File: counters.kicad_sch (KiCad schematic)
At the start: 20 parts, among them U10 74LV04, U11 74HC109, U12 74LV163, U13 74LV163, U14 74AHC30, U16 74VHC30, U18 74AHC30, U19 74VHC30, U20 74LV163, U21 74LV163, U22 74LV163, U23 74VHC30, U24 74HC109, U25 74VHC30, U26 74VHC30, U27 74VHC30, U28 74LV04, U29 74LV08, U8 74LV163, X1 25.175MHz

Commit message: cleanup
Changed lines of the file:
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@@
     (effects (font (size 1.27 1.27)) (justify left))
   )
-  (hierarchical_label "Row" (shape output) (at 261.62 69.85 0) (fields_autoplaced)
+  (hierarchical_label "Row[0..9]" (shape output) (at 261.62 69.85 0) (fields_autoplaced)
     (effects (font (size 1.27 1.27)) (justify left))
   )
@@
     (effects (font (size 1.27 1.27)) (justify left))
   )
-  (hierarchical_label "Col" (shape output) (at 133.35 71.12 0) (fields_autoplaced)
+  (hierarchical_label "Col[0..9]" (shape output) (at 133.35 71.12 0) (fields_autoplaced)
     (effects (font (size 1.27 1.27)) (justify left))
   )

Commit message: remove 3390, cleanup
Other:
- moved on the sheet: U12, U13, U20, U21, U22, U8

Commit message: misc fixes, start on pcb
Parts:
- removed unit 7 of U10
- removed unit 3 of U11
- removed unit 2 of U14
- removed unit 2 of U16
- removed unit 2 of U18
- removed unit 2 of U19
- removed unit 2 of U23
- removed unit 3 of U24
- removed unit 2 of U25
- removed unit 2 of U26
- removed unit 2 of U27
- removed unit 7 of U28
- removed unit 5 of U29
- added C1 (x7): 0.1u, Capacitor_SMD:C_1206_3216Metric_Pad1.33x1.80mm_HandSolder, symbol Device:C
- U10: renamed from U14; footprint (none) -> Package_SO:SOIC-14_3.9x8.7mm_P1.27mm
- U11: renamed from U18; footprint (none) -> Package_SO:SOIC-14_3.9x8.7mm_P1.27mm
- U12: renamed from U16; value 74VHC30 -> 74AHC30; footprint (none) -> Package_SO:SOIC-14_3.9x8.7mm_P1.27mm
- U13: renamed from U19; value 74VHC30 -> 74AHC30; footprint (none) -> Package_SO:SOIC-14_3.9x8.7mm_P1.27mm
- U14: renamed from U8; footprint (none) -> Package_SO:SOIC-16_3.9x9.9mm_P1.27mm
- U15: renamed from U10; footprint (none) -> Package_SO:SOIC-14_3.9x8.7mm_P1.27mm
- U16: renamed from U11; value 74HC109 -> 74AC109; footprint (none) -> Package_SO:SOIC-16_3.9x9.9mm_P1.27mm
- U17: renamed from U12; footprint (none) -> Package_SO:SOIC-16_3.9x9.9mm_P1.27mm
- U18: renamed from U28; footprint (none) -> Package_SO:SOIC-14_3.9x8.7mm_P1.27mm
- U19: renamed from U29; footprint (none) -> Package_SO:SOIC-14_3.9x8.7mm_P1.27mm
- U20: renamed from U13; footprint (none) -> Package_SO:SOIC-16_3.9x9.9mm_P1.27mm
- U21: renamed from U23; value 74VHC30 -> 74AHC30; footprint (none) -> Package_SO:SOIC-14_3.9x8.7mm_P1.27mm
- U22: renamed from U25; value 74VHC30 -> 74AHC30; footprint (none) -> Package_SO:SOIC-14_3.9x8.7mm_P1.27mm
- U23: renamed from U26; value 74VHC30 -> 74AHC30; footprint (none) -> Package_SO:SOIC-14_3.9x8.7mm_P1.27mm
- U24: renamed from U27; value 74VHC30 -> 74AHC30; footprint (none) -> Package_SO:SOIC-14_3.9x8.7mm_P1.27mm
- U25: renamed from U24; value 74HC109 -> 74AC109; footprint (none) -> Package_SO:SOIC-16_3.9x9.9mm_P1.27mm
- U26: renamed from U20; footprint (none) -> Package_SO:SOIC-16_3.9x9.9mm_P1.27mm
- U27: renamed from U21; footprint (none) -> Package_SO:SOIC-16_3.9x9.9mm_P1.27mm
- U28: renamed from U22; footprint (none) -> Package_SO:SOIC-16_3.9x9.9mm_P1.27mm
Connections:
- net +5V: now also C1.1, C1.1, C1.1, C1.1, C1.1, C1.1, C1.1
- net GND: now also C1.2, C1.2, C1.2, C1.2, C1.2, C1.2, C1.2
- net ~{HSync}: now reaches U16.9 (~{Q})
- net ~{VSync}: now reaches U25.9 (~{Q})
- net HSync: no longer names the net of U16.10 (Q)
- net VSync: no longer names the net of U25.10 (Q)
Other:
- note added: "Misc"
- note removed: "Power/Misc"
- moved on the sheet: X1

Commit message: pcb organization
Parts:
- added J10, J9: Conn_01x10, Connector_PinHeader_2.54mm:PinHeader_1x10_P2.54mm_Vertical, symbol Connector_Generic:Conn_01x10
- added J11, J12, J13, J14: Conn_01x03, Connector_PinHeader_2.54mm:PinHeader_1x03_P2.54mm_Vertical, symbol Connector_Generic:Conn_01x03
- added J16: Conn_01x01, Connector_PinHeader_2.54mm:PinHeader_1x01_P2.54mm_Vertical, symbol Connector_Generic:Conn_01x01
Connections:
- net Col0: now also J10.1 (Pin_1)
- net Col1: now also J10.2 (Pin_2)
- net Col2: now also J10.3 (Pin_3)
- net Col3: now also J10.4 (Pin_4)
- net Col4: now also J10.5 (Pin_5)
- net Col5: now also J10.6 (Pin_6)
- net Col6: now also J10.7 (Pin_7)
- net Col7: now also J10.8 (Pin_8)
- net Col8: now also J10.9 (Pin_9)
- net Col9: now also J10.10 (Pin_10)
- net HBlank: now also J11.1 (Pin_1)
- net HBlankClear: now also J11.3 (Pin_3)
- net HSyncSet: now also J12.2 (Pin_2)
- net PxClock: now also J16.1 (Pin_1)
- net Row0: now also J9.1 (Pin_1)
- net Row1: now also J9.2 (Pin_2)
- net Row2: now also J9.3 (Pin_3)
- net Row3: now also J9.4 (Pin_4)
- net Row4: now also J9.5 (Pin_5)
- net Row5: now also J9.6 (Pin_6)
- net Row6: now also J9.7 (Pin_7)
- net Row7: now also J9.8 (Pin_8)
- net Row8: now also J9.9 (Pin_9)
- net Row9: now also J9.10 (Pin_10)
- net VBlank: now also J13.1 (Pin_1)
- net VBlankSet: now also J13.2 (Pin_2)
- net VSyncSet: now also J14.2 (Pin_2)
- net ~{HBlankSet}: now also J11.2 (Pin_2)
- net ~{HSyncClear}: now also J12.3 (Pin_3)
- net ~{HSync}: now also J12.1 (Pin_1)
- net ~{VBlankClear}: now also J13.3 (Pin_3)
- net ~{VSyncClear}: now also J14.3 (Pin_3)
- net ~{VSync}: now also J14.1 (Pin_1)
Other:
- moved on the sheet: C1, U15E, U18E, U18F, U19D, X1

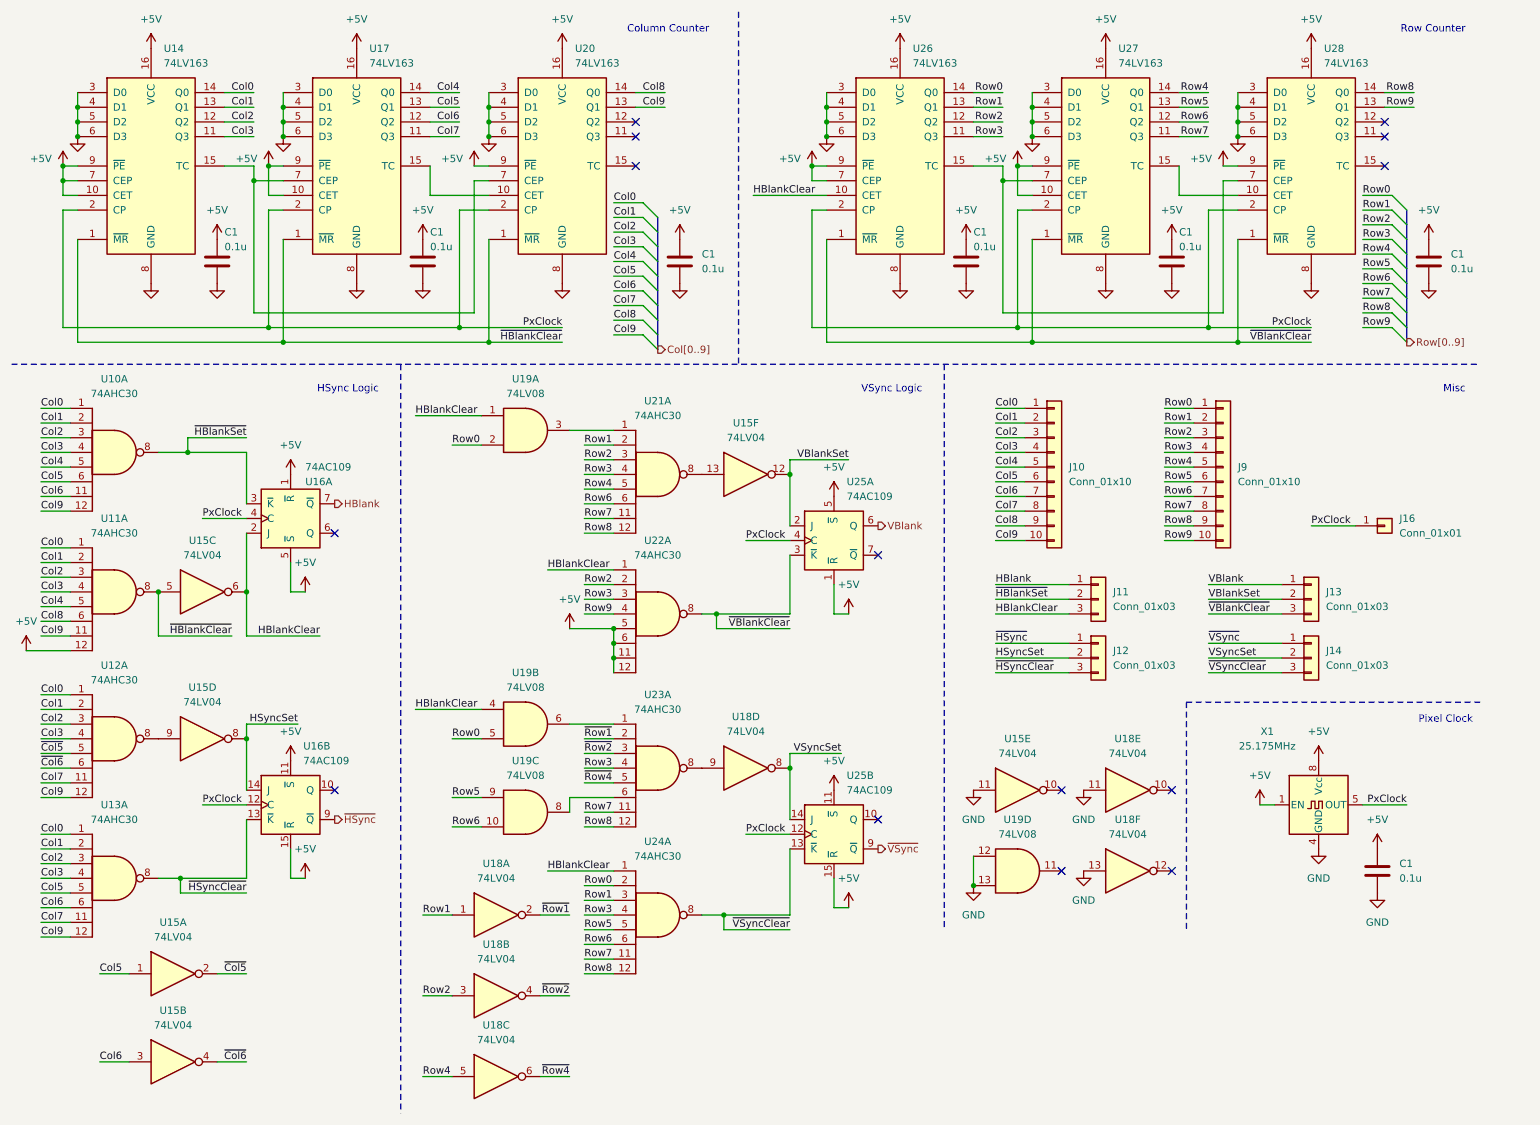
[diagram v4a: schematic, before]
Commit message: Suuuper dense routing for column counter
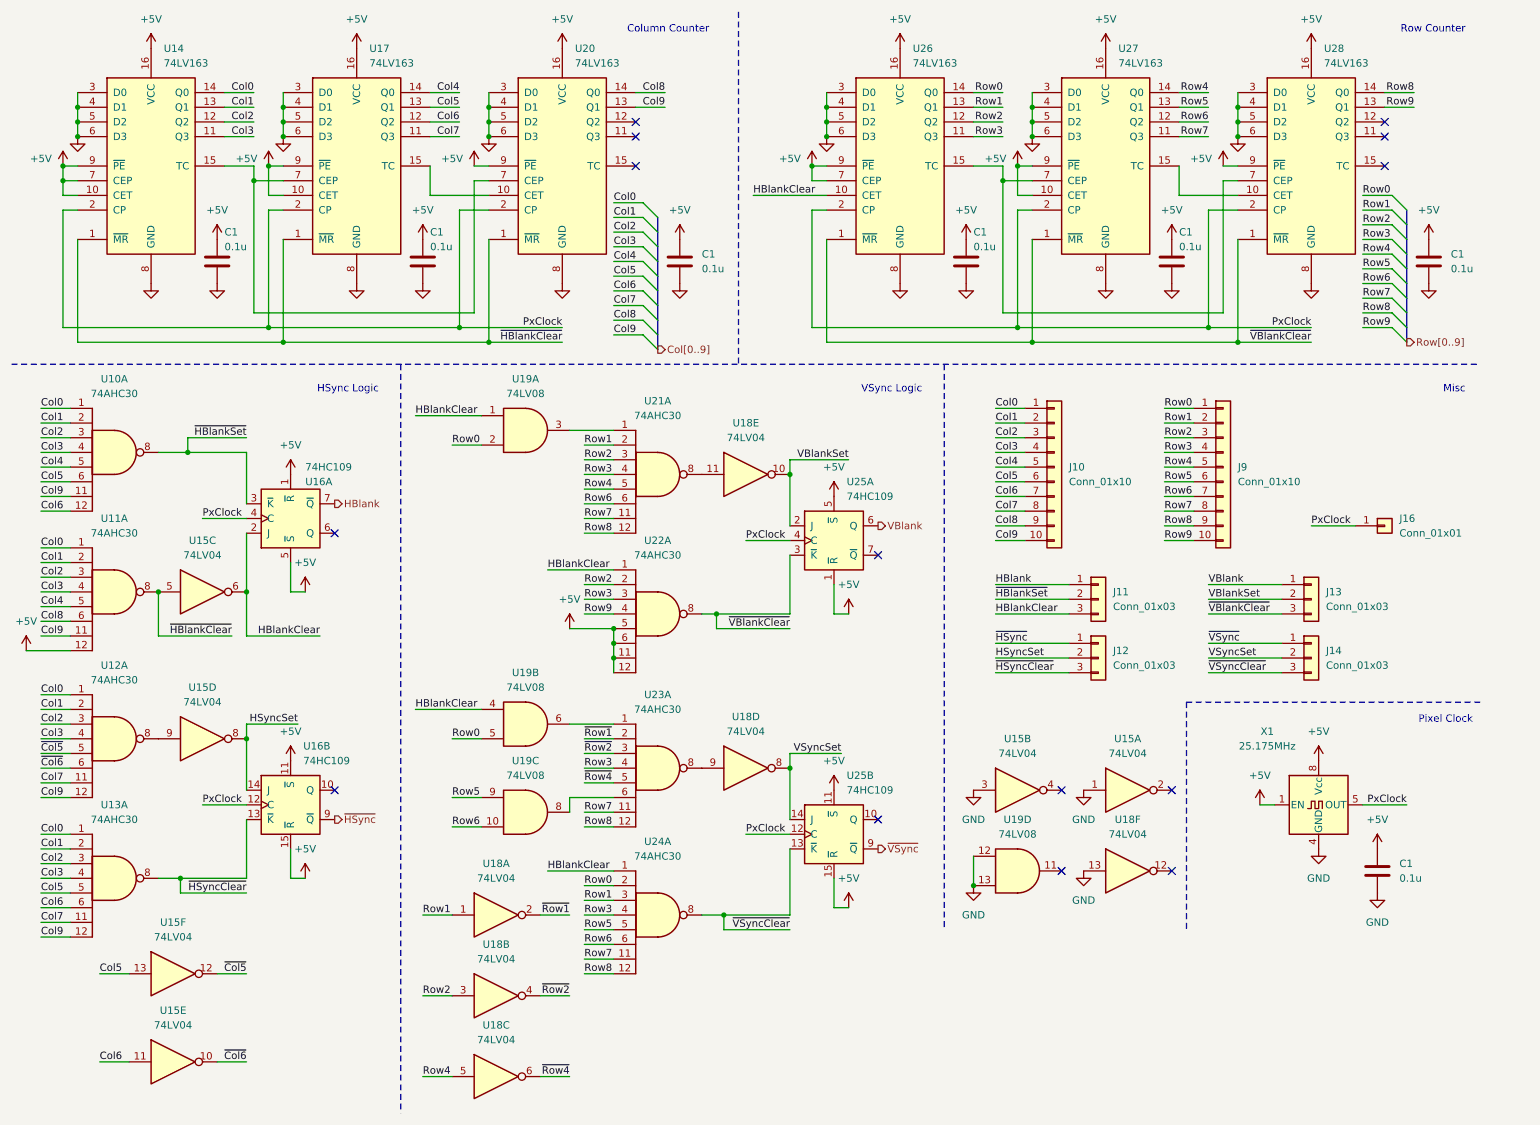
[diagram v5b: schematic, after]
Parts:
- U16, U25: value 74AC109 -> 74HC109
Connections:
- net Col5: now also U15.13; no longer U15.1
- net Col6: now also U10.12, U15.11; no longer U10.11, U15.3
- net Col9: now also U10.11; no longer U10.12
- net GND: now also U15.1, U15.3; no longer U15.11, U18.11
- net VBlankSet: now also U18.10; no longer U15.12
- net ~{Col5}: now also U15.12; no longer U15.2
- net ~{Col6}: now also U15.10; no longer U15.4
- net at U21.8: now also U18.11; no longer U15.13
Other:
- moved on the sheet: U15A, U15B, U15E, U15F, U18E

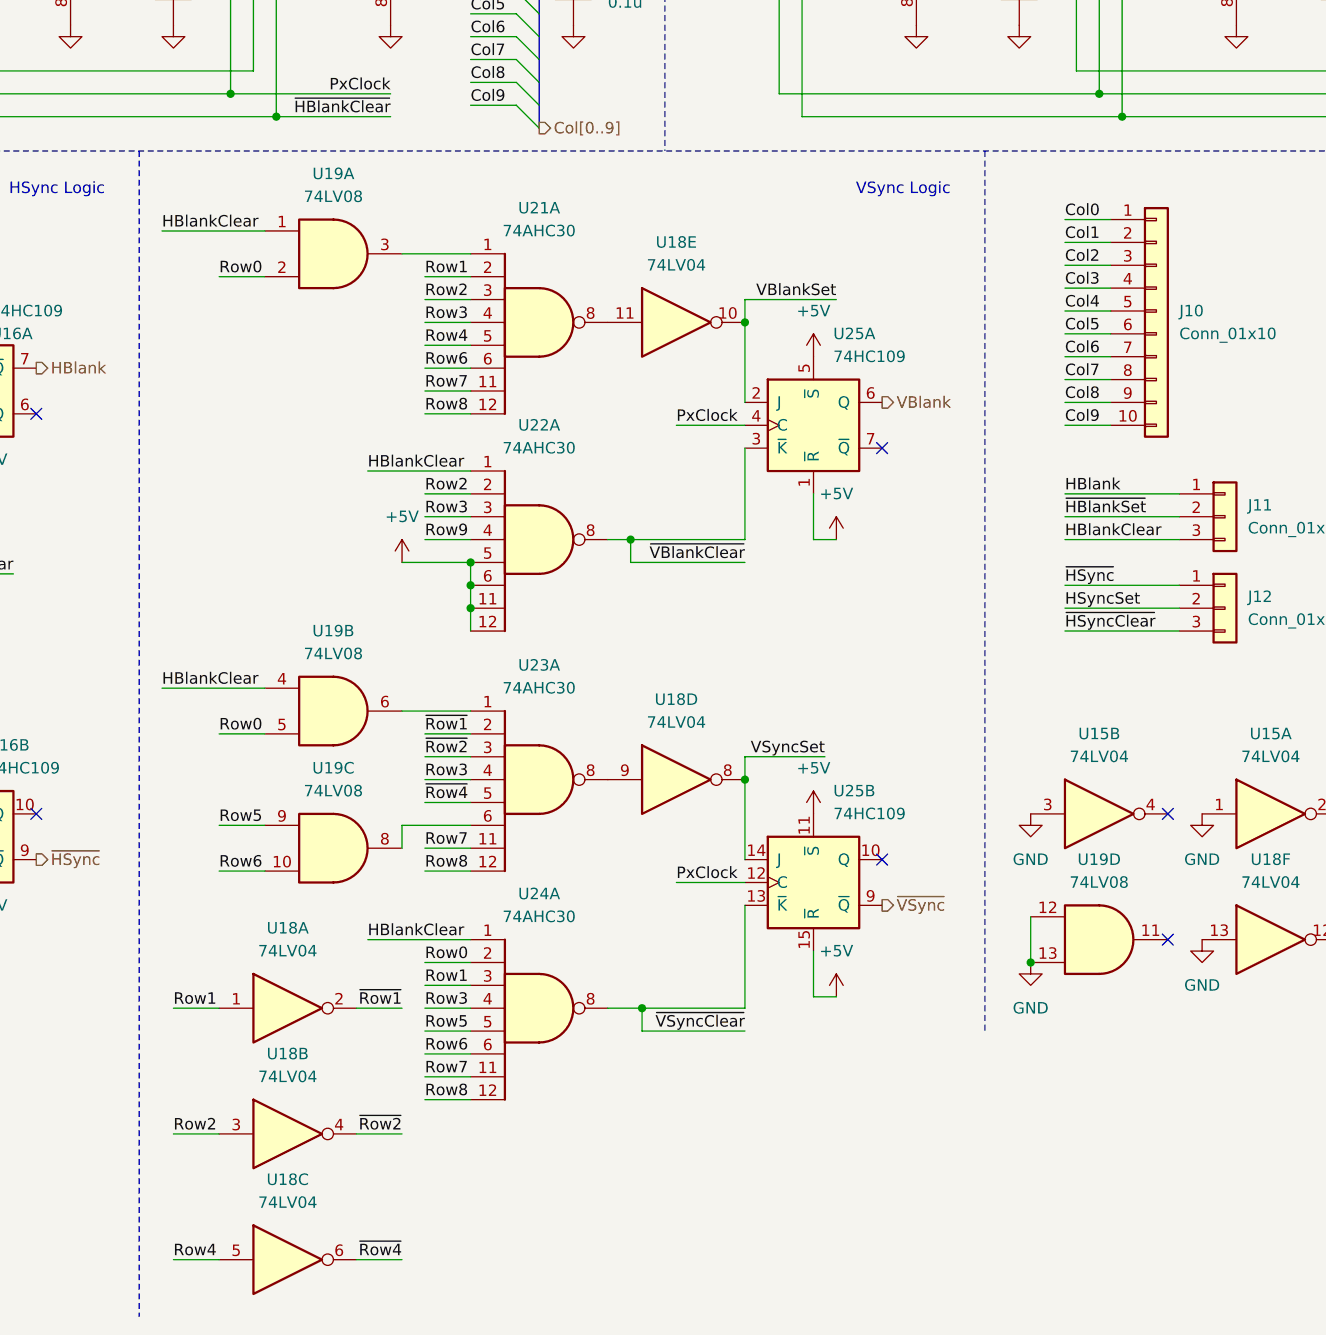
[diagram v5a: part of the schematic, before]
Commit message: Row counter logic
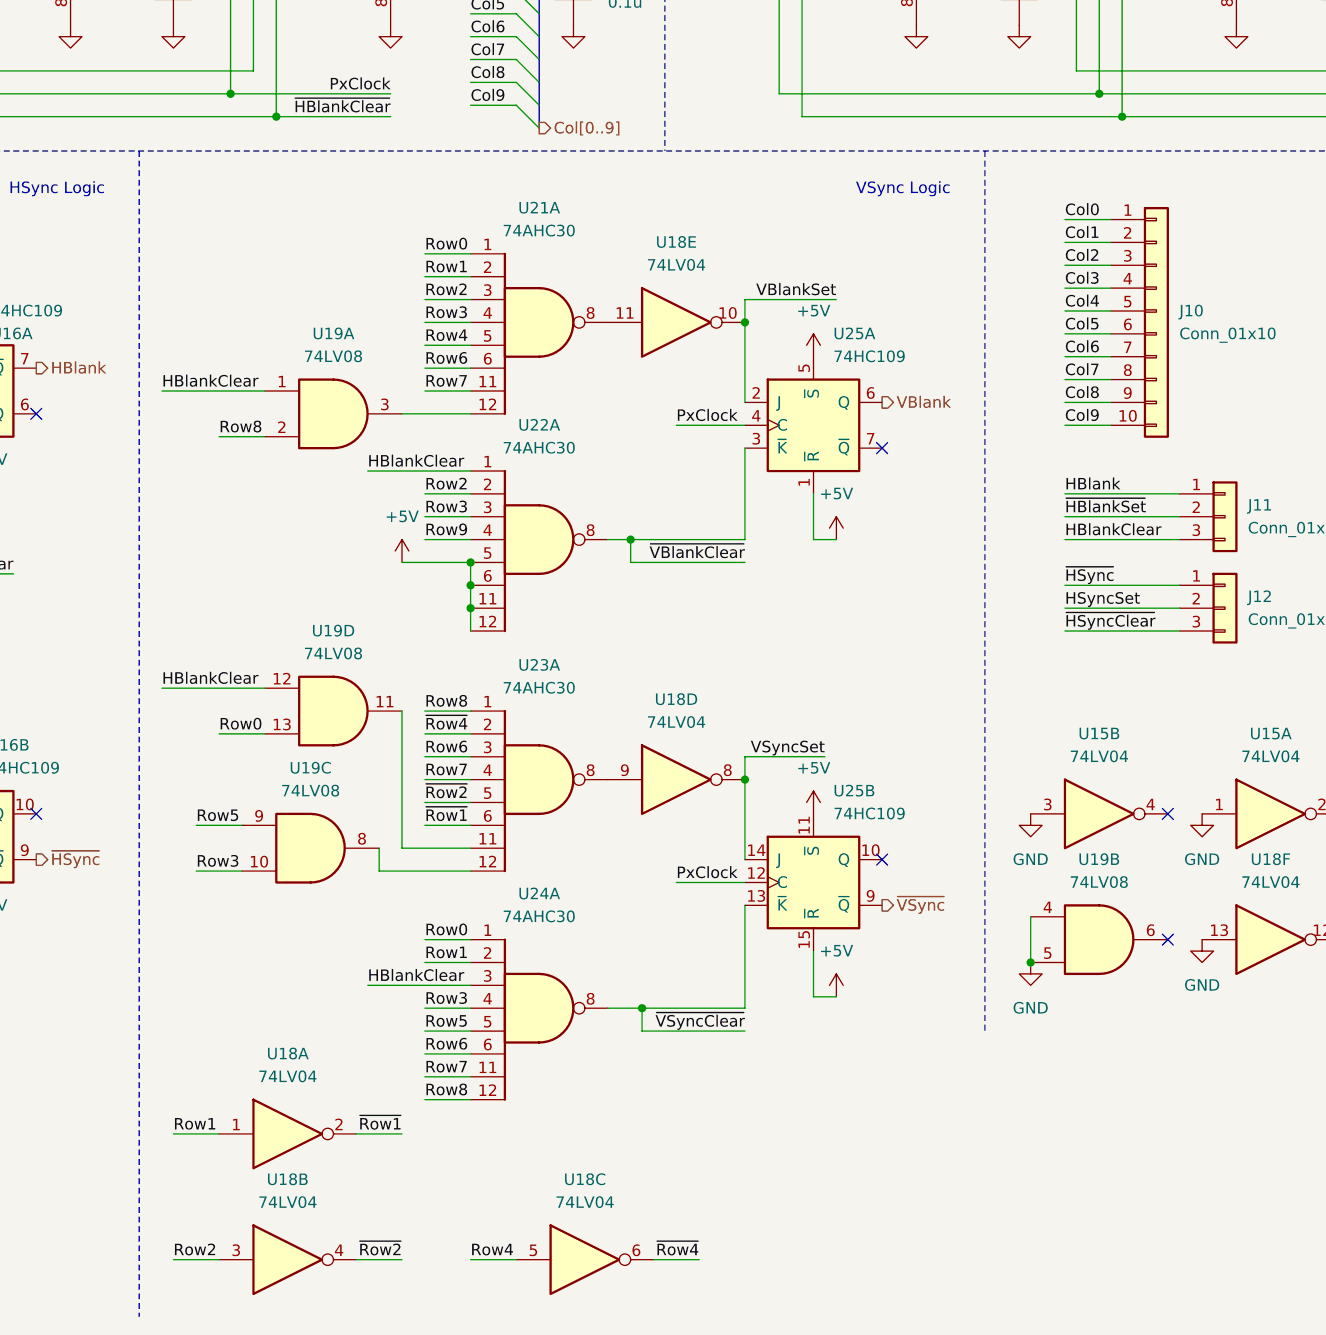
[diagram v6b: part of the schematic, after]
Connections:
- net GND: now also U19.4, U19.5; no longer U19.12, U19.13
- net HBlankClear: now also U19.12, U24.3; no longer U19.4, U24.1
- net Row0: now also U19.13, U21.1, U24.1; no longer U19.2, U19.5, U24.2
- net Row1: now also U24.2; no longer U24.3
- net Row3: now also U19.10; no longer U23.4
- net Row6: now also U23.3; no longer U19.10
- net Row7: now also U23.4; no longer U23.11
- net Row8: now also U19.2, U23.1; no longer U21.12, U23.12
- net ~{Row1}: now also U23.6; no longer U23.2
- net ~{Row2}: now also U23.5; no longer U23.3
- net ~{Row4}: now also U23.2; no longer U23.5
- net at U19.3: now also U21.12; no longer U21.1
- net at U19.11: now also U23.11
- net at U19.8: now also U23.12; no longer U23.6
- net at U19.6: no longer U23.1
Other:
- moved on the sheet: U18A, U18B, U18C, U19A, U19B, U19C, U19D

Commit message: Routing work
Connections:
- net HBlankClear: now also U21.1, U23.6; no longer U19.1, U19.12
- net Row0: now also U19.1; no longer U21.1
- net Row6: now also U23.2; no longer U23.3
- net Row7: now also U23.3; no longer U23.4
- net Row8: now also U19.12; no longer U23.1
- net ~{Row1}: now also U23.5; no longer U23.6
- net ~{Row2}: now also U23.4; no longer U23.5
- net ~{Row4}: now also U23.1; no longer U23.2
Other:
- moved on the sheet: U19C, U19D

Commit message: Memory routing *screams*
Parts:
- U16, U25: value 74HC109 -> 74AC109
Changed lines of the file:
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@@
       (effects (font (size 1.27 1.27)) (justify left))
     )
-    (property "Value" "74HC109" (at 63.1541 142.24 0)
+    (property "Value" "74AC109" (at 63.1541 142.24 0)
       (effects (font (size 1.27 1.27)) (justify left))
     )
@@
       (effects (font (size 1.27 1.27)) (justify left))
     )
-    (property "Value" "74HC109" (at 63.5 91.44 0)
+    (property "Value" "74AC109" (at 63.5 91.44 0)
       (effects (font (size 1.27 1.27)) (justify left))
     )
@@
       (effects (font (size 1.27 1.27)) (justify left))
     )
-    (property "Value" "74HC109" (at 157.1341 96.52 0)
+    (property "Value" "74AC109" (at 157.1341 96.52 0)
       (effects (font (size 1.27 1.27)) (justify left))
     )
@@
       (effects (font (size 1.27 1.27)) (justify left))
     )
-    (property "Value" "74HC109" (at 157.1341 147.32 0)
-      (effects (font (size 1.27 1.27)) (justify left))
-    )
+    (property "Value" "74AC109" (at 157.1341 147.32 0)
+      (effects (font (size 1.27 1.27)) (justify left))
+    )
